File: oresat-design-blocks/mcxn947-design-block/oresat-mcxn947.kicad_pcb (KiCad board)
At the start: 4 copper layers, 73.1 x 69.8 mm, 80 parts, among them J1 BKUP-BATT, J10 Conn_02x20_Odd_Even, J2 USB_C_Receptacle_USB2.0_14P, J3 CAN, J4 TERM, J5 10pin ARM SWD, J6 FTDI-UART-6PIN, J9 Conn_02x20_Odd_Even, SW1 RESET, SW2 ISP(BOOT), U1 MCXN947VKLT, U2 TCAN330, U3 TPS62111RSA, Y1 24 MHz, Y2 32.768 KHz

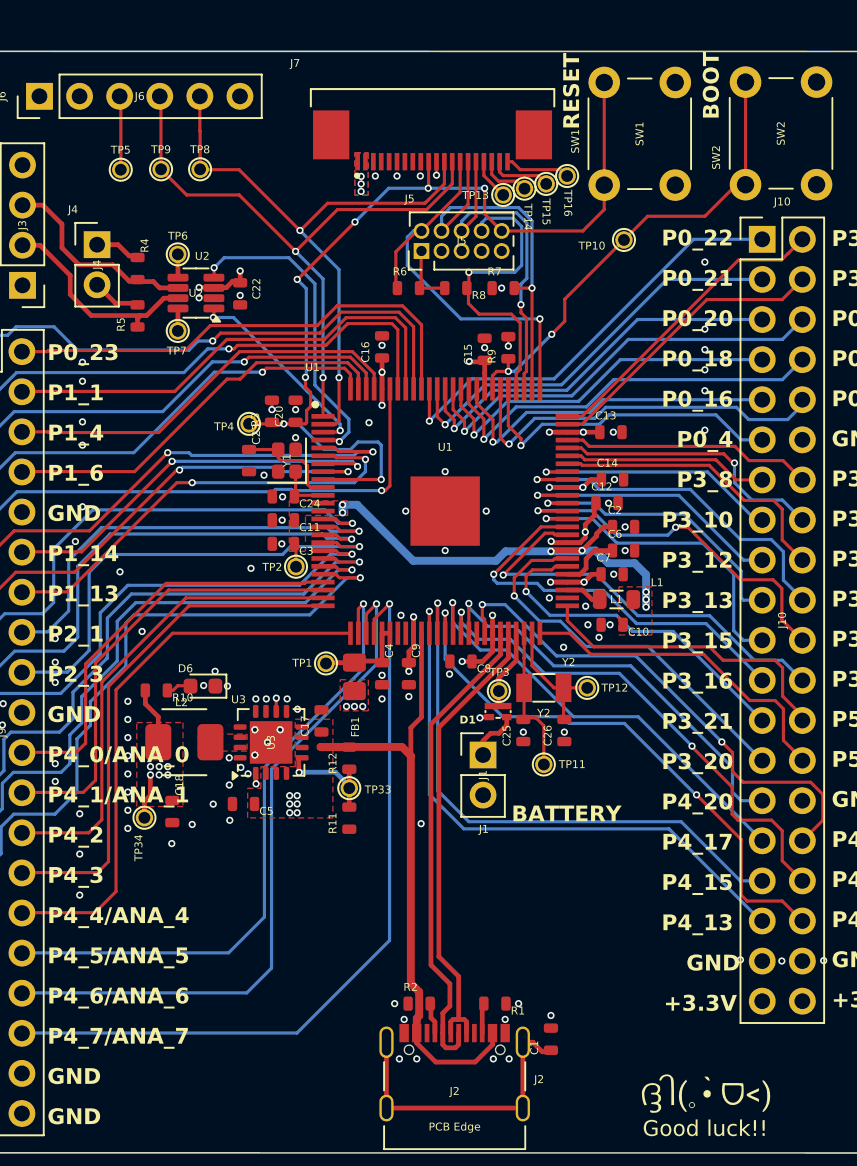
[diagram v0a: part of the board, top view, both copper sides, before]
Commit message: updated MCXN board with new cap footprints, cleaned up routes
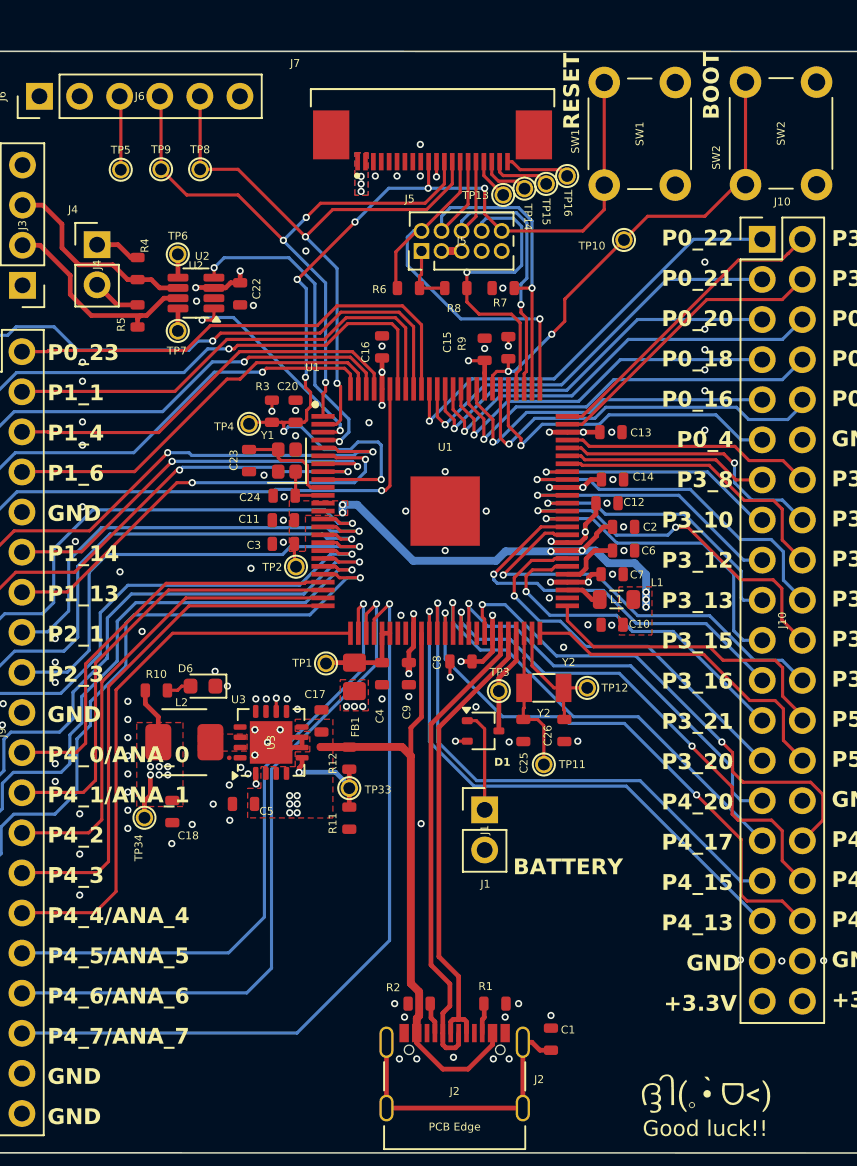
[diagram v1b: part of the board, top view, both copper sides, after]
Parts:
- D1: footprint oresat-passives:PAT0816(0603) -> Package_TO_SOT_SMD:SOT-323_SC-70
- moved J1 3.48 mm to (163.0, 119.6)
- moved D1 1.55 mm to (162.9, 114.6), turned to 0 degrees
- moved C24 0.07 mm to (150.3, 99.7)
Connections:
- J6 pad 4: ISP-UART_TXD -> ISP-UART_RXD
- J6 pad 5: ISP-UART_RXD -> ISP-UART_TXD
- TP8 pad 1: ISP-UART_RXD -> ISP-UART_TXD
- TP9 pad 1: ISP-UART_TXD -> ISP-UART_RXD
- U1 pad 1: ISP-UART_TXD -> ISP-UART_RXD
- U1 pad 2: ISP-UART_RXD -> ISP-UART_TXD
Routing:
- net GND: track 5.94 -> 12.8 mm, vias 104 -> 103
- net Net-(J1-Pin_1): track 3.33 -> 6.44 mm
- net P4_13: track 37.5 -> 35.5 mm
- net +3.3V: track 58.0 -> 59.9 mm
- net P4_15: track 36.7 -> 34.9 mm
- net Net-(U1C-P1_10): track 13.0 -> 14.6 mm
- net Net-(U1A-VDD_BAT): track 5.09 -> 6.64 mm
- net ISP-UART_RXD: track 38.5 -> 39.7 mm, vias 2 -> 3
- net ISP-UART_TXD: track 39.6 -> 38.9 mm
- net RESET: track 60.5 -> 61.0 mm

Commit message: Last minute polishing / DRC cleanup / nice work Anna!
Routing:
- net GND: vias 103 -> 102
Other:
- board text added: "BLK"

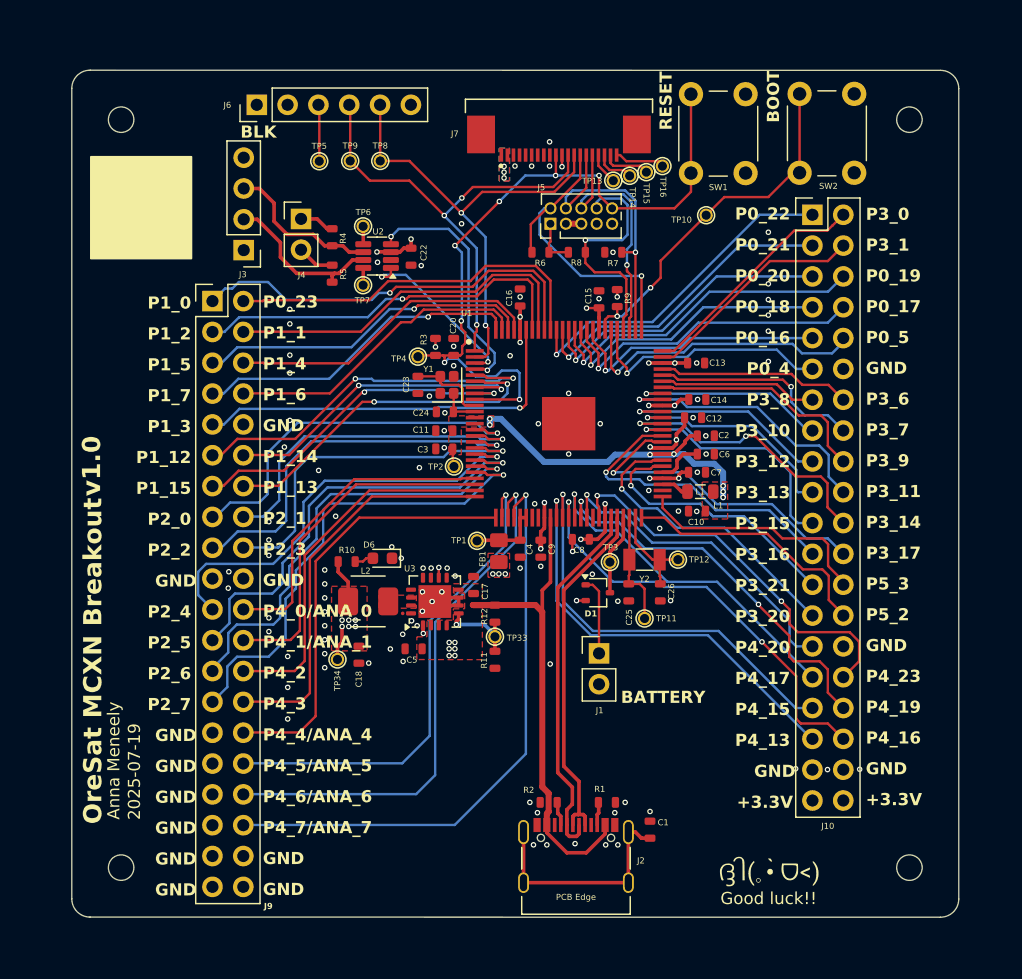
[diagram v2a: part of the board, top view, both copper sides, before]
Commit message: Updated BOM with MPNs and fixed one missing 0805 footprint error, rev'd board to v1.1
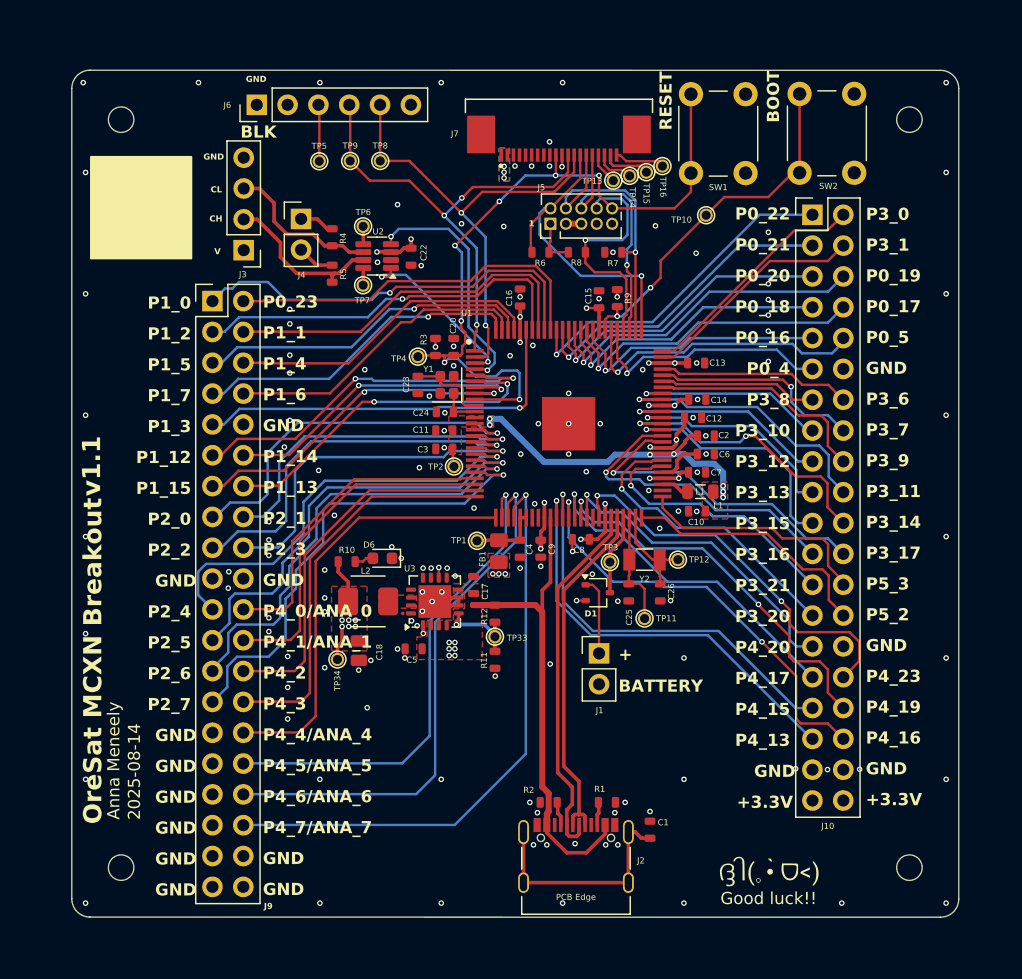
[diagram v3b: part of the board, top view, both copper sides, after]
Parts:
- C18: footprint oresat-passives:0603-C-NOSILK -> oresat-passives:0805-C-NOSILK
- FB1: value 120 ohm ? -> 120 ohm
- J7: value ~ -> OreSat Debug
- moved C18 0.33 mm to (143.2, 119.4)
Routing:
- net GND: vias 102 -> 140
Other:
- board text added: "+"
- board text added: "1"
- board text added: "CH"
- board text added: "CL"
- board text added: "V"

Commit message: oops forgot to update PCB
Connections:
- net /Power & Signal/BOOT renamed /Signals and Breakouts/BOOT
- net /Power & Signal/CANH renamed /Signals and Breakouts/CANH
- net /Power & Signal/CANL renamed /Signals and Breakouts/CANL

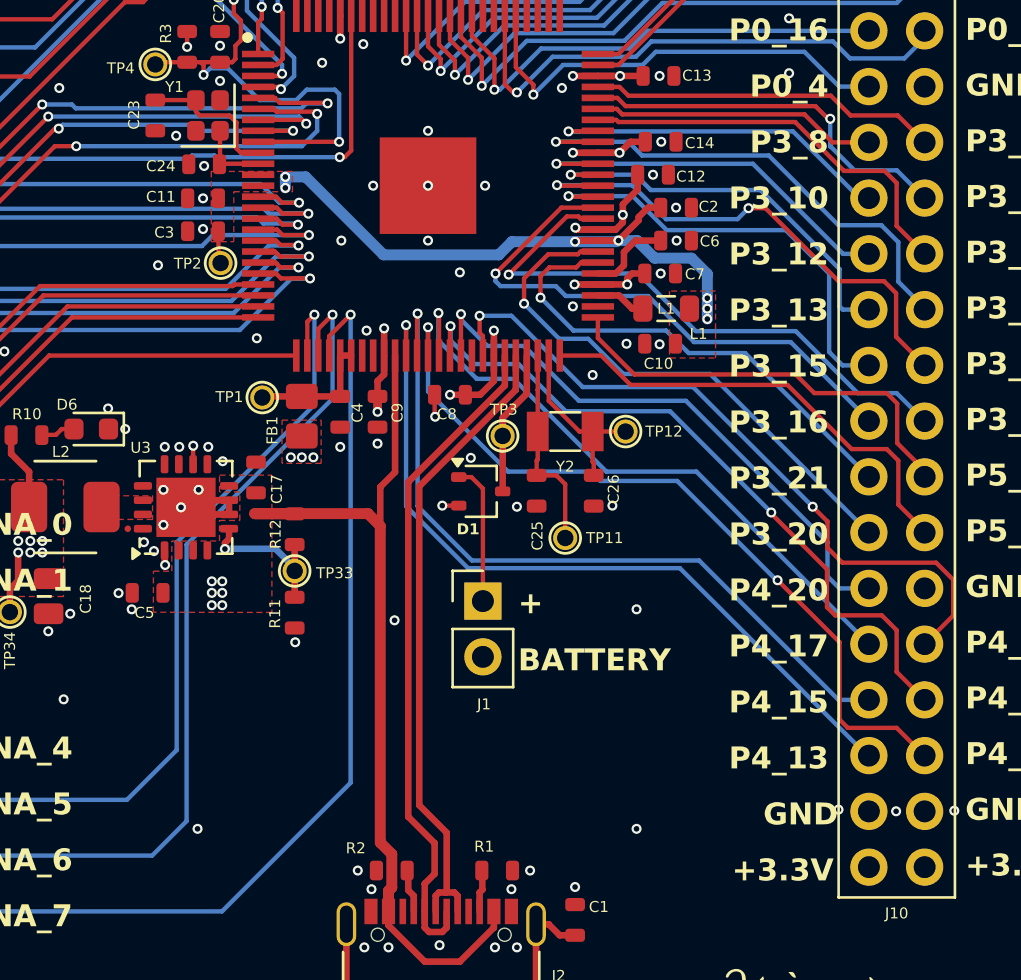
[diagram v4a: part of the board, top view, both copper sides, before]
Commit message: Fixed MCXN center pad paste, re-arranged MCXN power pins, and fixed breakout board to hopefully not short.
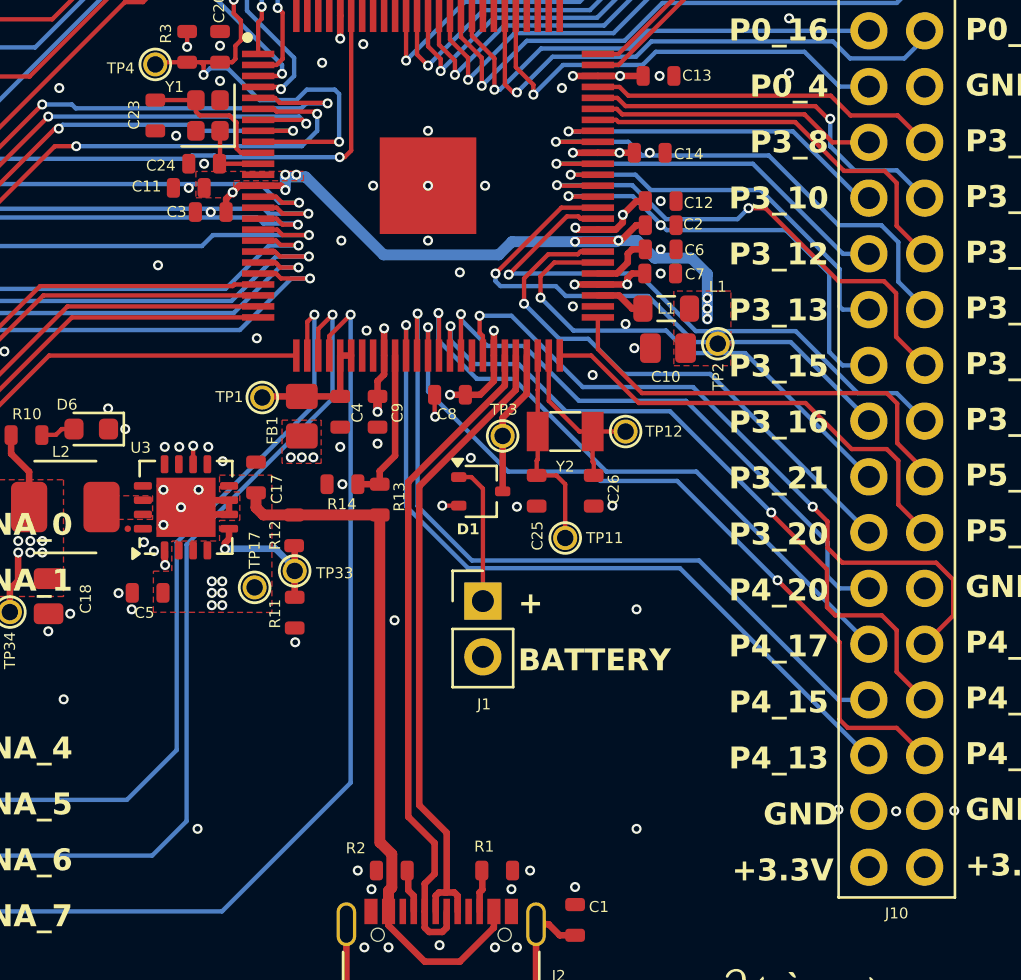
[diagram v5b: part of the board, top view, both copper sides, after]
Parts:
- added R13: 15k, oresat-passives:0603-C-NOSILK, F.Cu at (158.3, 115.0)
- added R14: 10k, oresat-passives:0603-C-NOSILK, F.Cu at (156.6, 114.3)
- added TP17: Test-Point, oresat-misc:TestPoint-0.75mm-th, F.Cu at (152.6, 119.0)
- C10: footprint oresat-passives:0603-C-NOSILK -> oresat-passives:0805-C-NOSILK
- moved TP2 22.9 mm to (173.7, 107.9), turned to 90 degrees
- moved C12 1.25 mm to (171.1, 101.4)
- moved C2 1.06 mm to (171.1, 102.5)
- moved C3 0.94 mm to (150.6, 101.9)
- moved C6 0.81 mm to (171.1, 103.6)
- moved C11 0.81 mm to (149.6, 100.8)
- moved C14 0.71 mm to (170.6, 99.2)
- moved C10 0.41 mm to (171.4, 108.1)
- moved R12 0.06 mm to (154.4, 116.4)
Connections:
- net Net-(U1A-VDD_ANA) renamed /Power and Ext Connectors/VDD_ANA
- net Net-(U1A-VDD_BAT) renamed /Power and Ext Connectors/VDD_BAT
- net Net-(U1A-VDD_SYS) renamed /Power and Ext Connectors/VDD_SYS
- C10 pad 1: VDD -> VDD_CORE
- C11 pad 1: VDD -> VDD_CORE
- C2 pad 1: VDD -> VDD_CORE
- C3 pad 1: VDD -> +3.3V
- L1 pad 1: VDD -> VDD_CORE
- TP2 pad 1: VDD -> VDD_CORE
- U1 pad 12: VDD -> VDD_CORE
- U1 pad 13: VDD -> +3.3V
- U1 pad 35: VBUS -> /Signals and Breakouts/USB0_VUS_DET
- U1 pad 58: VDD -> VDD_CORE
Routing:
- net VDD: track 30.2 -> 0.00 mm, vias 7 -> 0
- net VDD_CORE: track 0.00 -> 27.6 mm, vias 0 -> 7
- net VBUS: track 119.3 -> 110.4 mm
- net /Signals and Breakouts/USB0_VUS_DET: track 0.00 -> 7.15 mm
- net +3.3V: track 59.9 -> 62.0 mm, vias 31 -> 33
- net /Power and Ext Connectors/VDD_SYS: track 3.83 -> 2.85 mm
- net GND: vias 140 -> 141
- added copper zone on F.Cu, net VDD_CORE
- removed copper zone on F.Cu, net VDD

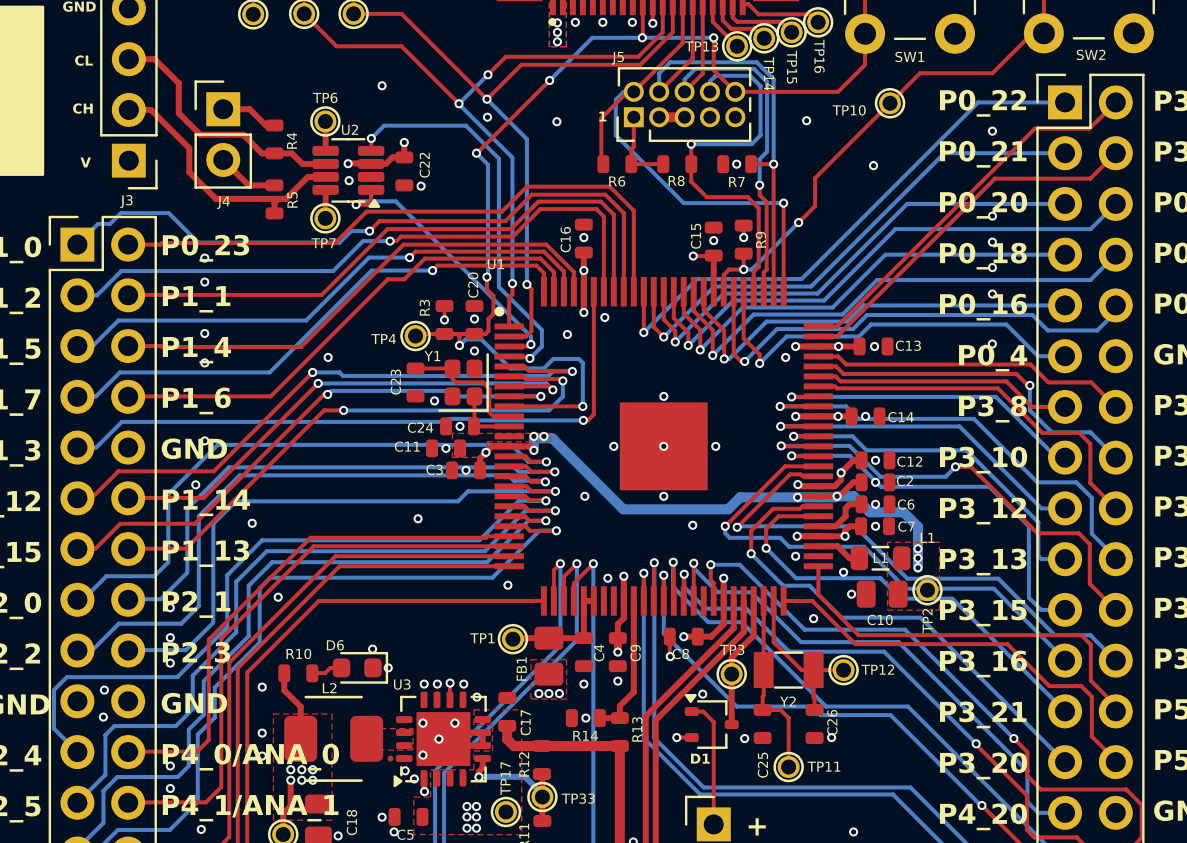
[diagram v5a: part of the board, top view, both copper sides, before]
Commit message: Lots of DRC cleanup - why were there so many shorting errors?! Maybe this was never really checked. Added capacitor for bypass on MCXN pin.
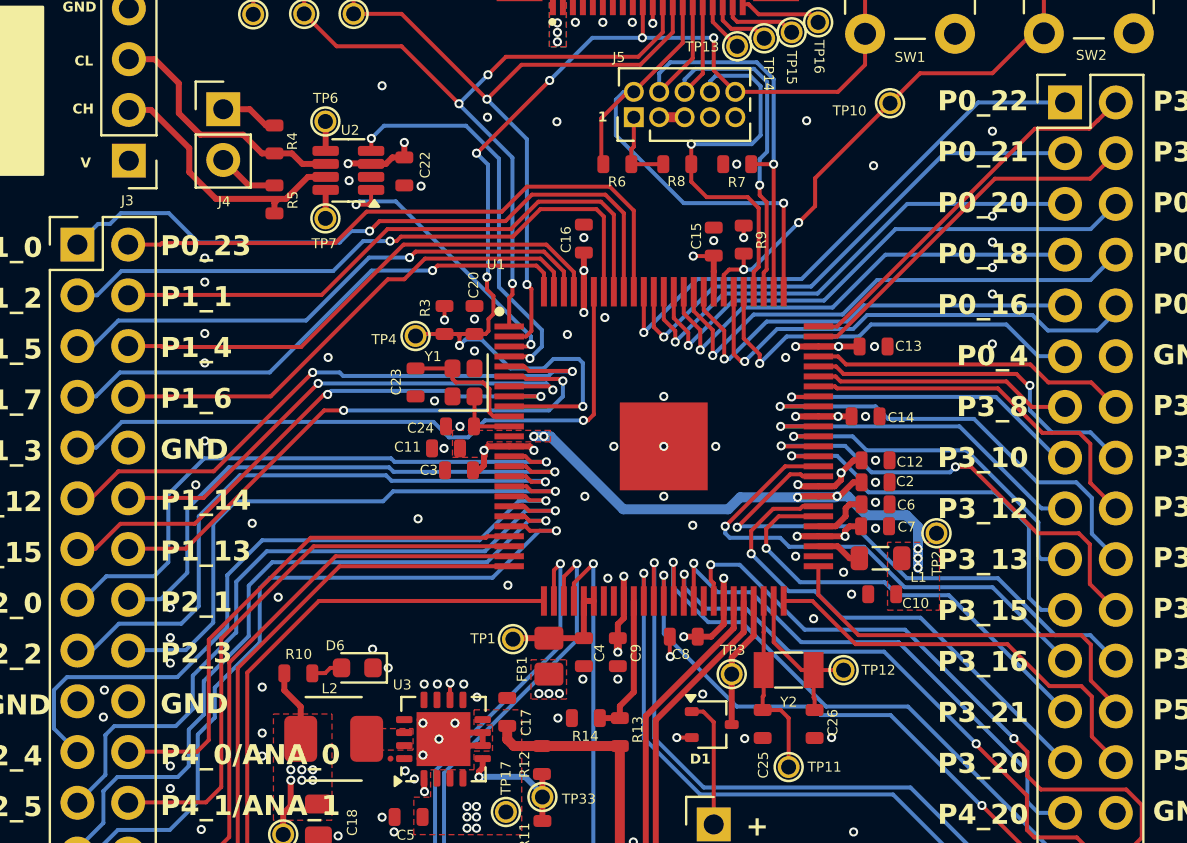
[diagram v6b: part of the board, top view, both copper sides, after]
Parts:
- C10: footprint oresat-passives:0805-C-NOSILK -> oresat-passives:0603-C-NOSILK
- moved TP2 2.89 mm to (174.2, 105.0)
- moved C3 0.35 mm to (150.2, 101.9)
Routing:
- net P1_3: track 32.7 -> 33.3 mm
- net Net-(J9-Pin_15): track 31.0 -> 30.4 mm
- net GND: vias 141 -> 140
